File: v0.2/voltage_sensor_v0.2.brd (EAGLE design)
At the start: 77 x 105 mm, 59 parts, among them IC1 AP2112K-3.3TRG1, J2 236-404_000-009_999-950, J3 MC000048, J9 RJ11, T1 ZMPT101B, T2 ZMPT101B, T3 ZMPT101B

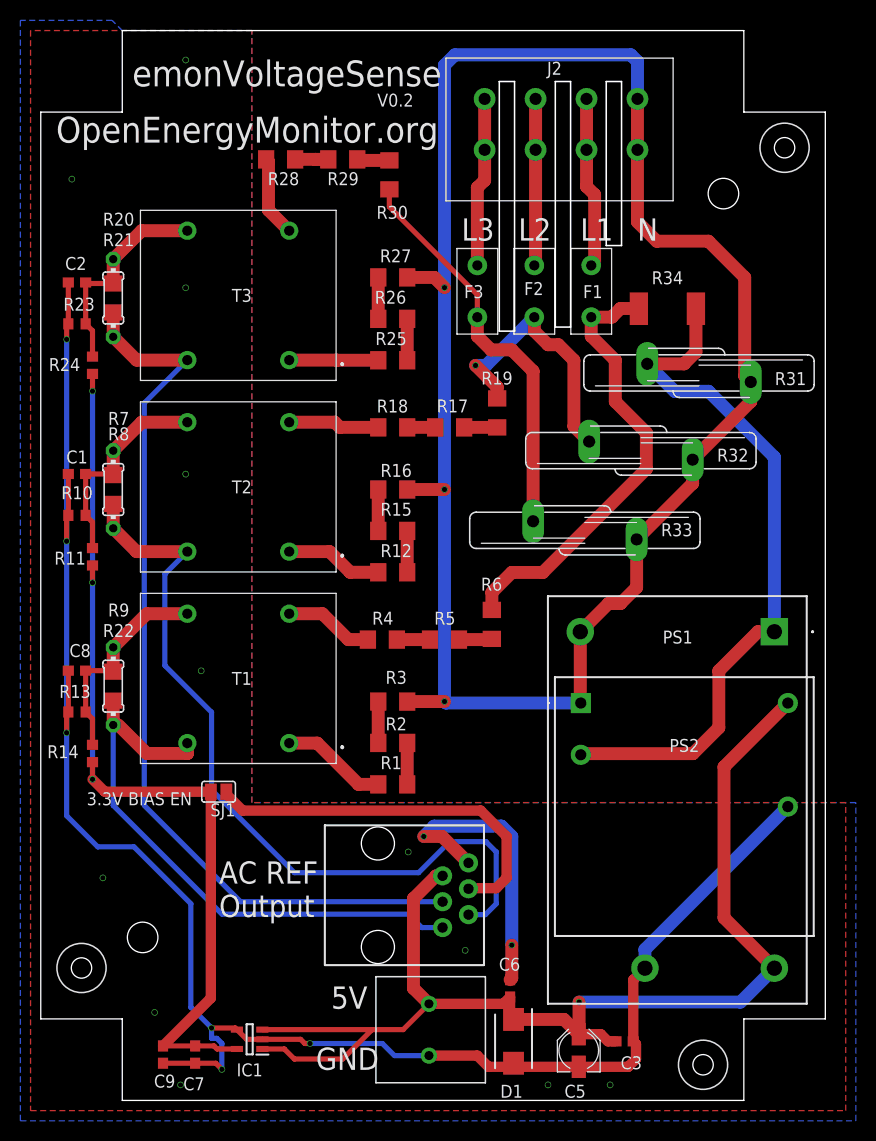
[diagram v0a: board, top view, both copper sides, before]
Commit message: fix resistor footprint and value
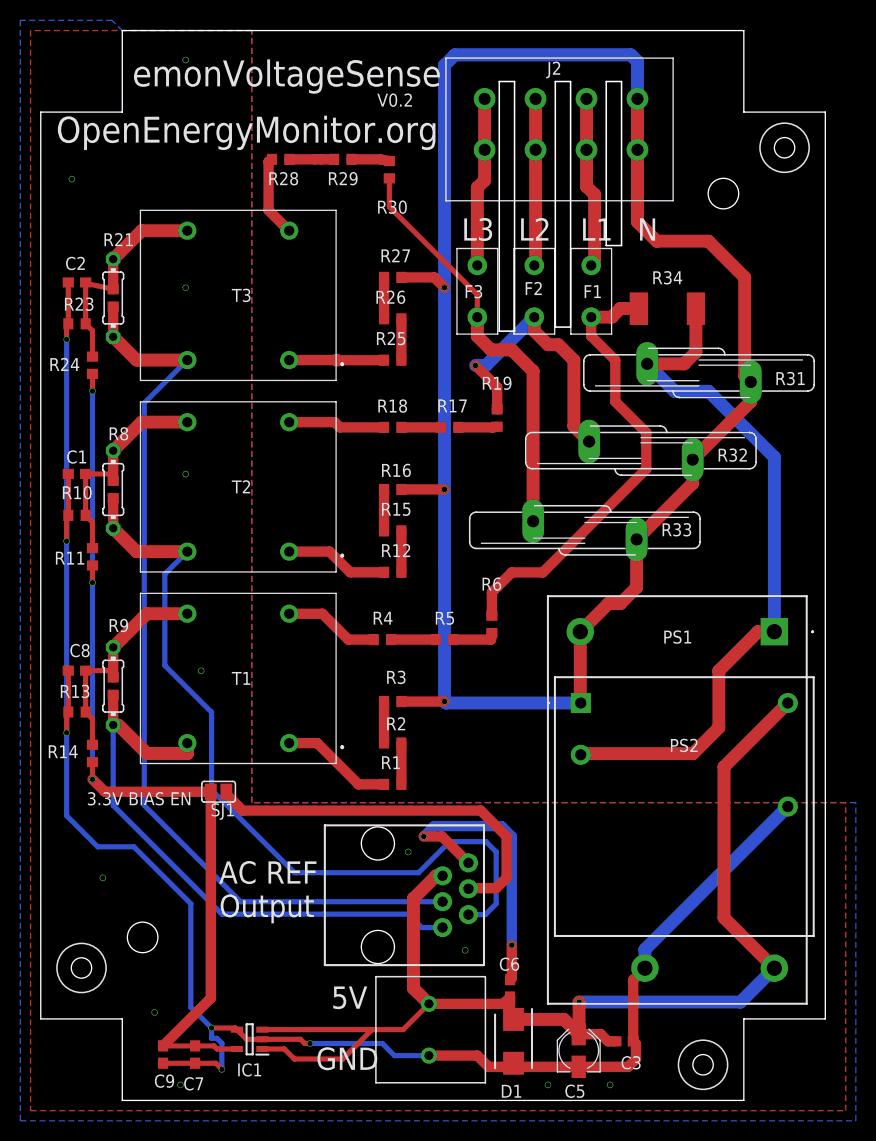
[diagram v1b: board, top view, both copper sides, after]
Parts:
- R1, R12, R15, R16, R17, R18, R19, R2, R25, R26, R27, R28, R29, R3, R30, R4, R5, R6: value (none) -> 10k; device rcl:R1206 -> rcl:R0603
- R21, R8, R9: value (none) -> 75R; device rcl:R1206 -> rcl:R0603
- moved R19 0.51 mm to (44.8, 67.0)
- moved R30 0.51 mm to (34.2, 91.3)
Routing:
- net NEUTRAL: track 185.1 -> 186.8 mm
- net N$4: track 3.25 -> 4.40 mm
- net N$22: track 3.25 -> 4.40 mm
- net N$13: track 2.74 -> 3.89 mm
- net N$5: track 3.25 -> 4.37 mm
- net N$25: track 21.3 -> 22.4 mm
- net N$9: track 21.1 -> 22.2 mm
- net L3: track 39.6 -> 40.7 mm
- net L2: track 26.9 -> 28.0 mm
- net N$18: track 21.1 -> 21.8 mm
- net N$14: track 3.24 -> 3.82 mm
- net VS3: track 89.3 -> 89.8 mm
- net VS2: track 78.0 -> 78.6 mm
- net VS1: track 57.0 -> 57.6 mm
- net N$19: track 8.74 -> 9.32 mm
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
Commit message: improve clearance
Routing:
- net N$17: track 70.2 -> 66.3 mm
- net 5V: track 120.4 -> 117.5 mm
- net L2: track 28.0 -> 25.6 mm
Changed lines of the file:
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@@
 <wire x1="49.784" y1="74.168" x2="48.436" y2="75.516" width="1.27" layer="1"/>
 <wire x1="48.436" y1="75.516" x2="48.436" y2="76.872" width="1.27" layer="1"/>
-<wire x1="48.436" y1="76.872" x2="43.7" y2="72.136" width="1.27" layer="16"/>
-<wire x1="43.7" y1="72.136" x2="42.672" y2="72.136" width="1.27" layer="16"/>
-<via x="42.672" y="72.136" extent="1-16" drill="0.5"/>
-<wire x1="42.672" y1="72.136" x2="44.796" y2="70.012" width="1.016" layer="1"/>
-<wire x1="44.796" y1="70.012" x2="44.796" y2="67.818" width="1.016" layer="1"/>
+<wire x1="48.436" y1="76.872" x2="48.436" y2="74.332" width="1.016" layer="16"/>
+<wire x1="48.436" y1="74.332" x2="45.732" y2="71.628" width="1.016" layer="16"/>
+<wire x1="45.732" y1="71.628" x2="45.72" y2="71.628" width="1.016" layer="16"/>
+<wire x1="45.72" y1="71.628" x2="45.212" y2="71.12" width="1.016" layer="16"/>
+<via x="45.212" y="71.12" extent="1-16" drill="0.5"/>
+<wire x1="45.212" y1="71.12" x2="44.796" y2="70.704" width="1.016" layer="1"/>
+<wire x1="44.796" y1="70.704" x2="44.796" y2="67.818" width="1.016" layer="1"/>
 </signal>
 <signal name="L3">
@@
 <contactref element="D1" pad="1"/>
 <contactref element="J3" pad="2"/>
-<wire x1="72" y1="12.98" x2="67.056" y2="17.924" width="1.27" layer="1"/>
-<wire x1="67.056" y1="32.736" x2="73.32" y2="39" width="1.27" layer="1"/>
-<wire x1="67.056" y1="17.924" x2="67.056" y2="32.736" width="1.27" layer="1"/>
+<wire x1="72" y1="12.98" x2="70.612" y2="14.368" width="1.27" layer="1"/>
+<wire x1="70.612" y1="36.292" x2="73.32" y2="39" width="1.27" layer="1"/>
+<wire x1="70.612" y1="14.368" x2="70.612" y2="36.292" width="1.27" layer="1"/>
 <wire x1="52.8" y1="6.5" x2="54.968" y2="6.5" width="1.016" layer="1"/>
 <wire x1="55.668" y1="5.8" x2="56.45" y2="5.8" width="1.016" layer="1"/>
@@
 <wire x1="63.145" y1="72.289" x2="59.52" y2="72.289" width="1.27" layer="1"/>
 <wire x1="64.3" y1="73.444" x2="63.145" y2="72.289" width="1.27" layer="1"/>
-<wire x1="72" y1="46" x2="72" y2="63.128" width="1.27" layer="16"/>
+<wire x1="72" y1="46" x2="72" y2="62.112" width="1.27" layer="16"/>
 <wire x1="62.213" y1="69.596" x2="59.52" y2="72.289" width="1.27" layer="16"/>
-<wire x1="72" y1="63.128" x2="65.532" y2="69.596" width="1.27" layer="16"/>
-<wire x1="65.532" y1="69.596" x2="62.213" y2="69.596" width="1.27" layer="16"/>
+<wire x1="72" y1="62.112" x2="64.516" y2="69.596" width="1.27" layer="16"/>
+<wire x1="64.516" y1="69.596" x2="62.213" y2="69.596" width="1.27" layer="16"/>
 <wire x1="53" y1="33.92" x2="53.116" y2="34.036" width="1.27" layer="1"/>
-<wire x1="53.116" y1="34.036" x2="64.008" y2="34.036" width="1.27" layer="1"/>
-<wire x1="64.008" y1="34.036" x2="66.548" y2="36.576" width="1.27" layer="1"/>
-<wire x1="66.548" y1="36.576" x2="66.548" y2="42.164" width="1.27" layer="1"/>
-<wire x1="66.548" y1="42.164" x2="70.384" y2="46" width="1.27" layer="1"/>
+<wire x1="53.116" y1="34.036" x2="58.42" y2="34.036" width="1.27" layer="1"/>
+<wire x1="58.42" y1="34.036" x2="70.384" y2="46" width="1.27" layer="1"/>
 <wire x1="70.384" y1="46" x2="72" y2="46" width="1.27" layer="1"/>
 </signal>
